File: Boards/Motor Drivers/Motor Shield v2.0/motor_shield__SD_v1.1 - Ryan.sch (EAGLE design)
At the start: 25 parts

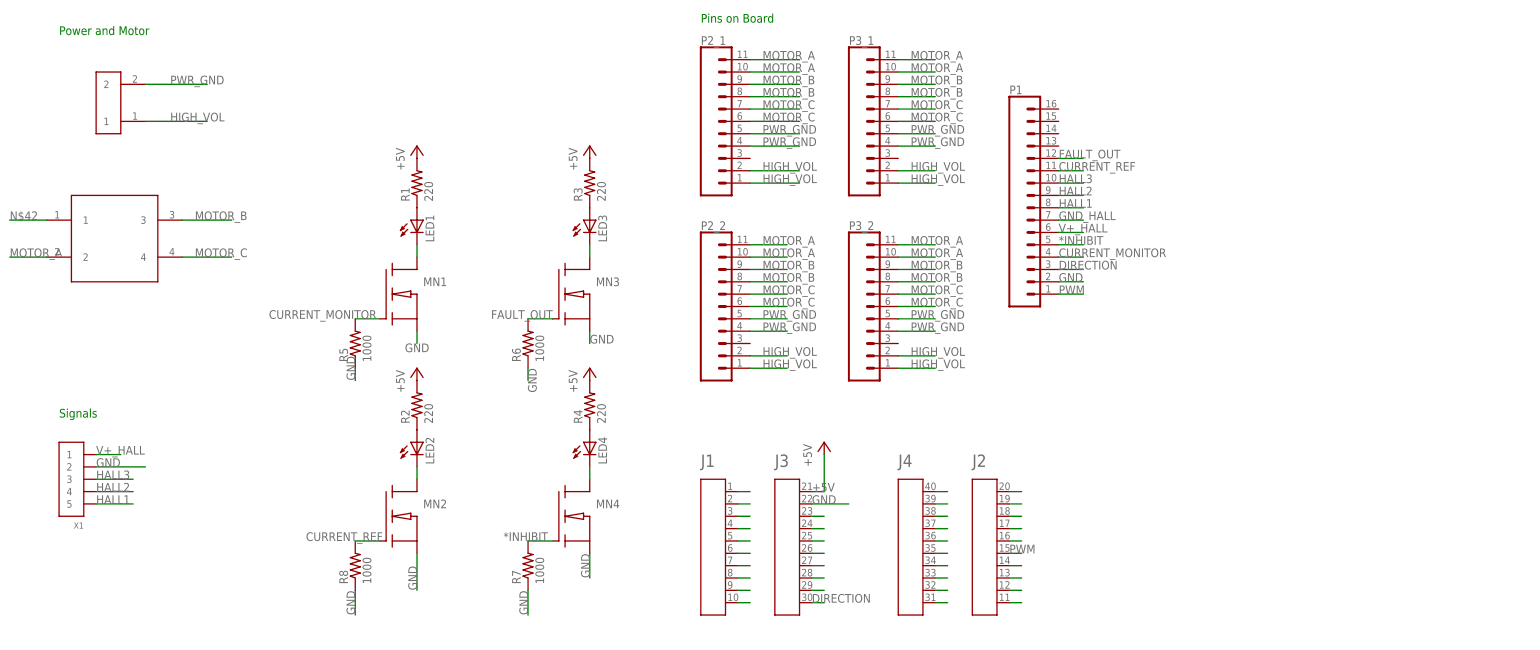
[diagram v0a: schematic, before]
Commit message: Changes tiva headers, corrected ground and vol connections, layout finalizing. started routing
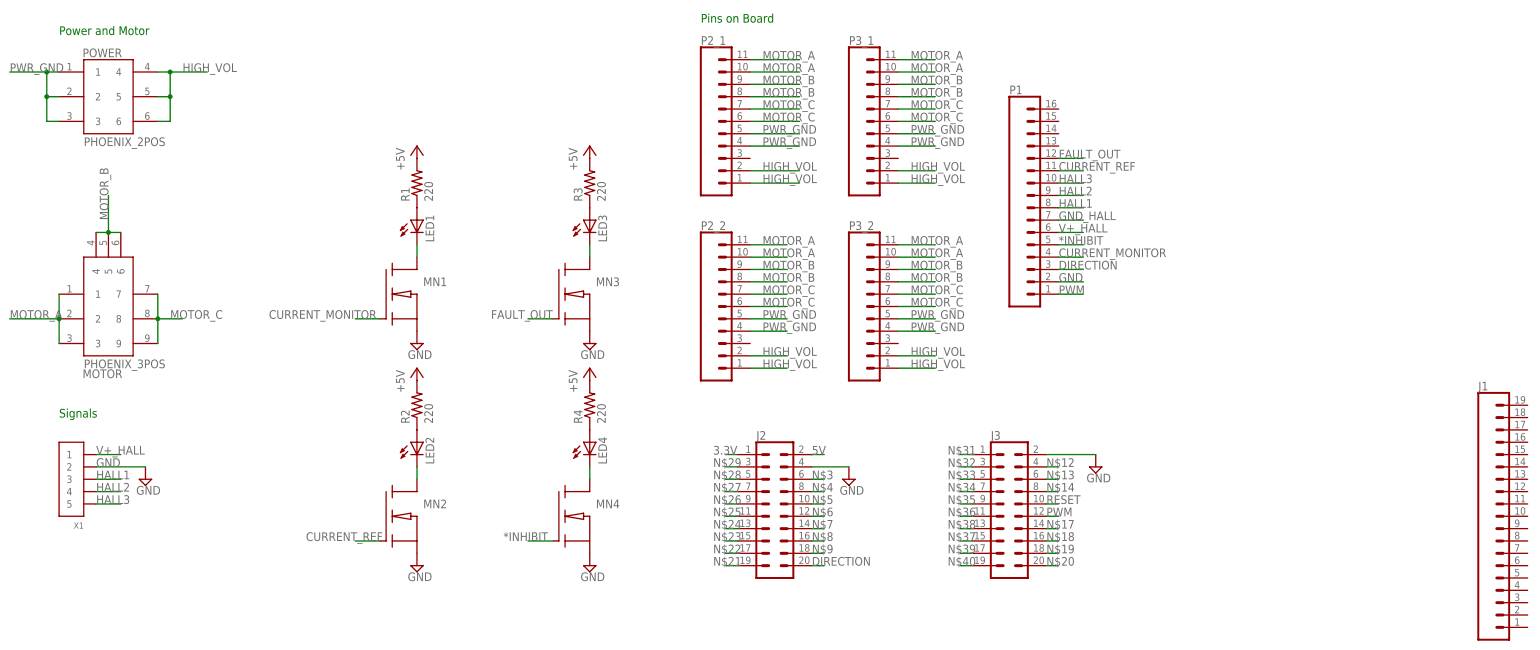
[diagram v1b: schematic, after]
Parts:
- removed A1: (no value), EAGLE_BoosterPack_Library:HEADER4X10-BOOSTERPACK
- removed R5, R6, R7, R8: 1000, adafruit:R-US_R0603
- removed U$1: MOLEX2CON, TREC:MOLEX2CON
- removed U$2: MOLEX4CON, TREC1:MOLEX4CON
- added J1: (no value), SparkFun-Connectors:CONN_19
- added J2, J3: (no value), SparkFun-Connectors:CONN_10X2
- added MOTOR: PHOENIX_3POS, phoenixConn_3POS:PHOENIX_3POS
- added POWER: PHOENIX_2POS, phoenixConn_2POS:PHOENIX_2POS
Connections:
- removed net N$42: U$2.1
- removed net N$46: A1.P$1
- removed net N$47: A1.P$2
- removed net N$48: A1.P$3
- removed net N$49: A1.P$4
- removed net N$50: A1.P$5
- removed net N$51: A1.P$6
- removed net N$52: A1.P$7
- removed net N$53: A1.P$8
- removed net N$54: A1.P$9
- removed net N$55: A1.P$10
- removed net N$58: A1.P$23
- removed net N$59: A1.P$24
- removed net N$60: A1.P$25
- removed net N$61: A1.P$26
- removed net N$62: A1.P$27
- removed net N$63: A1.P$28
- removed net N$64: A1.P$29
- removed net N$66: A1.P$40
- removed net N$67: A1.P$39
- removed net N$68: A1.P$38
- removed net N$69: A1.P$37
- removed net N$70: A1.P$36
- removed net N$71: A1.P$35
- removed net N$72: A1.P$34
- removed net N$73: A1.P$33
- removed net N$74: A1.P$32
- removed net N$75: A1.P$31
- removed net N$76: A1.P$20
- removed net N$77: A1.P$19
- removed net N$78: A1.P$18
- removed net N$79: A1.P$17
- removed net N$80: A1.P$16
- removed net N$82: A1.P$14
- removed net N$83: A1.P$13
- removed net N$84: A1.P$12
- removed net N$85: A1.P$11
- new net 3.3V: J2.1
- new net 5V: J2.2
- new net N$12: J3.4
- new net N$13: J3.6
- new net N$14: J3.8
- new net N$17: J3.14
- new net N$18: J3.16
- new net N$19: J3.18
- new net N$20: J3.20
- new net N$21: J2.19
- new net N$22: J2.17
- new net N$23: J2.15
- new net N$24: J2.13
- new net N$25: J2.11
- new net N$26: J2.9
- new net N$27: J2.7
- new net N$28: J2.5
- new net N$29: J2.3
- new net N$3: J2.6
- new net N$31: J3.1
- new net N$32: J3.3
- new net N$33: J3.5
- new net N$34: J3.7
- new net N$35: J3.9
- new net N$36: J3.11
- new net N$37: J3.15
- new net N$38: J3.13
- new net N$39: J3.17
- new net N$4: J2.8
- new net N$40: J3.19
- new net N$5: J2.10
- new net N$6: J2.12
- new net N$7: J2.14
- new net N$8: J2.16
- new net N$9: J2.18
- new net RESET: J3.10
- net *INHIBIT: no longer R7.2
- net +5V: no longer A1.P$21
- net CURRENT_MONITOR: no longer R5.2
- net CURRENT_REF: no longer R8.2
- net DIRECTION: now also J2.20; no longer A1.P$30
- net FAULT_OUT: no longer R6.2
- net GND: now also J2.4, J3.2; no longer A1.P$22, R5.1, R6.1, R7.1, R8.1
- net HALL1: now also X1.3; no longer X1.5
- net HALL3: now also X1.5; no longer X1.3
- net HIGH_VOL: now also POWER.4, POWER.5, POWER.6; no longer U$1.1
- net MOTOR_A: now also MOTOR.1, MOTOR.2, MOTOR.3; no longer U$2.2
- net MOTOR_B: now also MOTOR.4, MOTOR.5, MOTOR.6; no longer U$2.3
- net MOTOR_C: now also MOTOR.7, MOTOR.8, MOTOR.9; no longer U$2.4
- net PWM: now also J3.12; no longer A1.P$15
- net PWR_GND: now also POWER.1, POWER.2, POWER.3; no longer U$1.2
